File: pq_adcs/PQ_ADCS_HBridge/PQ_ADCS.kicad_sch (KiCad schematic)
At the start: 53 parts, among them J1 CES-110-02-L-S, J10 Pico-Clasp_01x09, J11 Pico-Clasp_01x15, J12 CES-102-02-L-S, J2 CES-110-02-L-S, J3 CES-110-02-L-S, J4 CES-110-02-L-S, J5 Pico-Clasp_01x03, J6 Pico-Clasp_01x10, J7 Pico-Clasp_01x10, J8 Pico-Clasp_01x10, J9 Pico-Clasp_01x10, U1 LPV542, U2 LPV542, U3 LPV542, U4 IIM-42652, U5 DRV8214RTER, U6 TMUX1108RSVR, U7 MMC5983MA, U8 DRV8214RTER, U9 DRV8214RTER

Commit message: NC digital pincs fix
Unused digital pins as well as I2C pins are now set as not connected instead of grounded. Added lock files to gitignore
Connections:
- net GND: no longer U5.3 (RC_OUT), U5.4 (~{FAULT}), U8.3 (RC_OUT), U8.4 (~{FAULT}), U9.3 (RC_OUT), U9.4 (~{FAULT})
- no-connect marks 9 -> 18

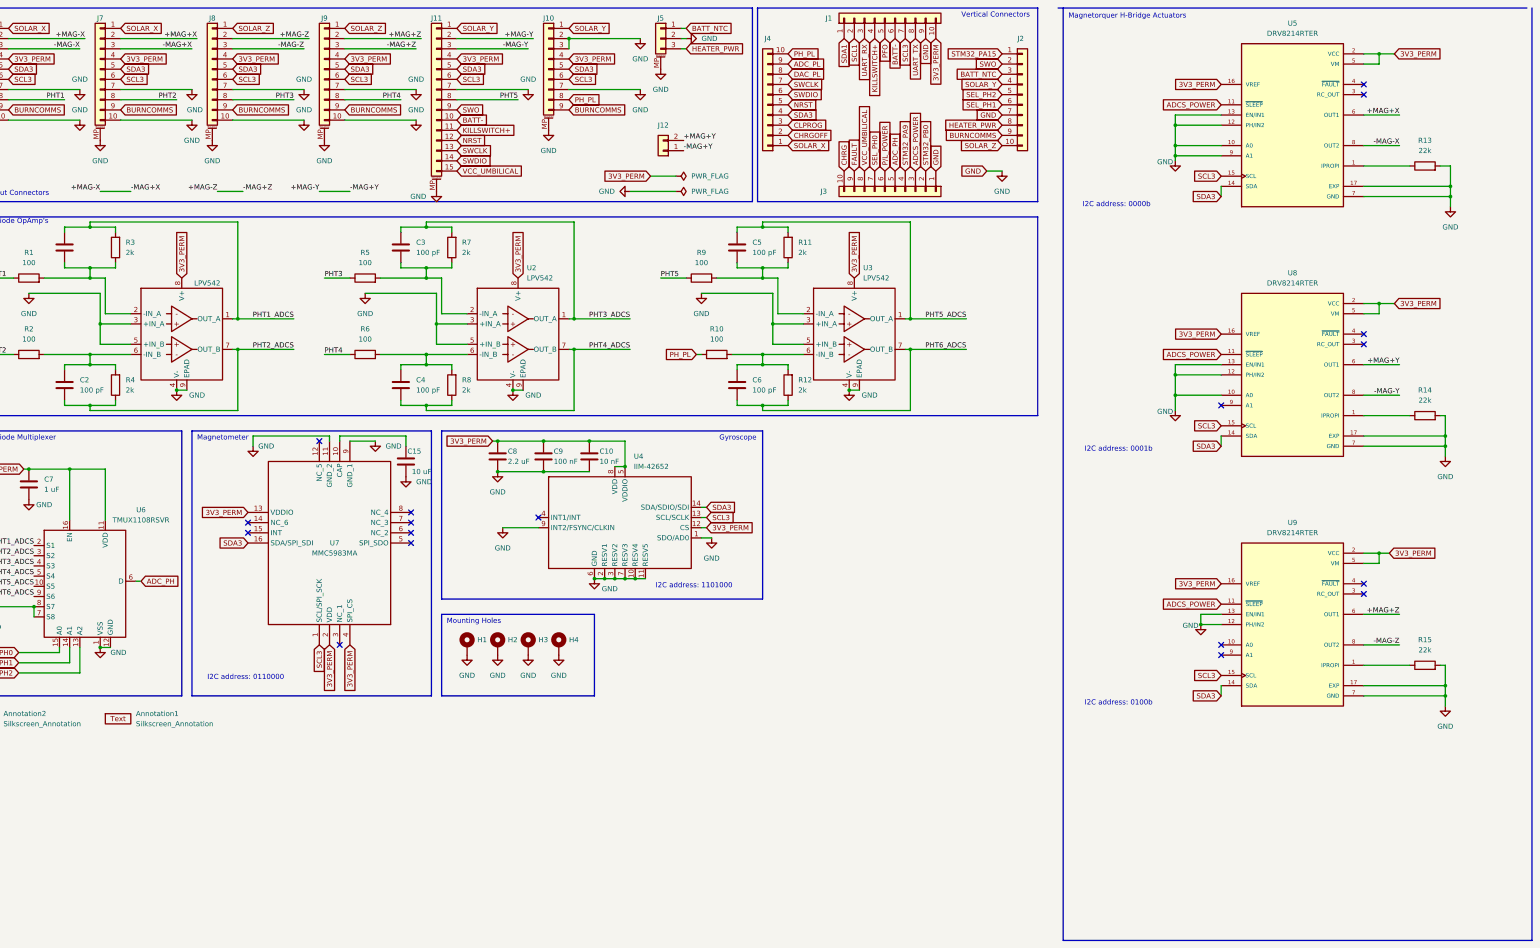
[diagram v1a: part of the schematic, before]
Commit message: Added Capacitors to HBridge Controllers
Coupling capacitors added as required by the HBridge controllers.
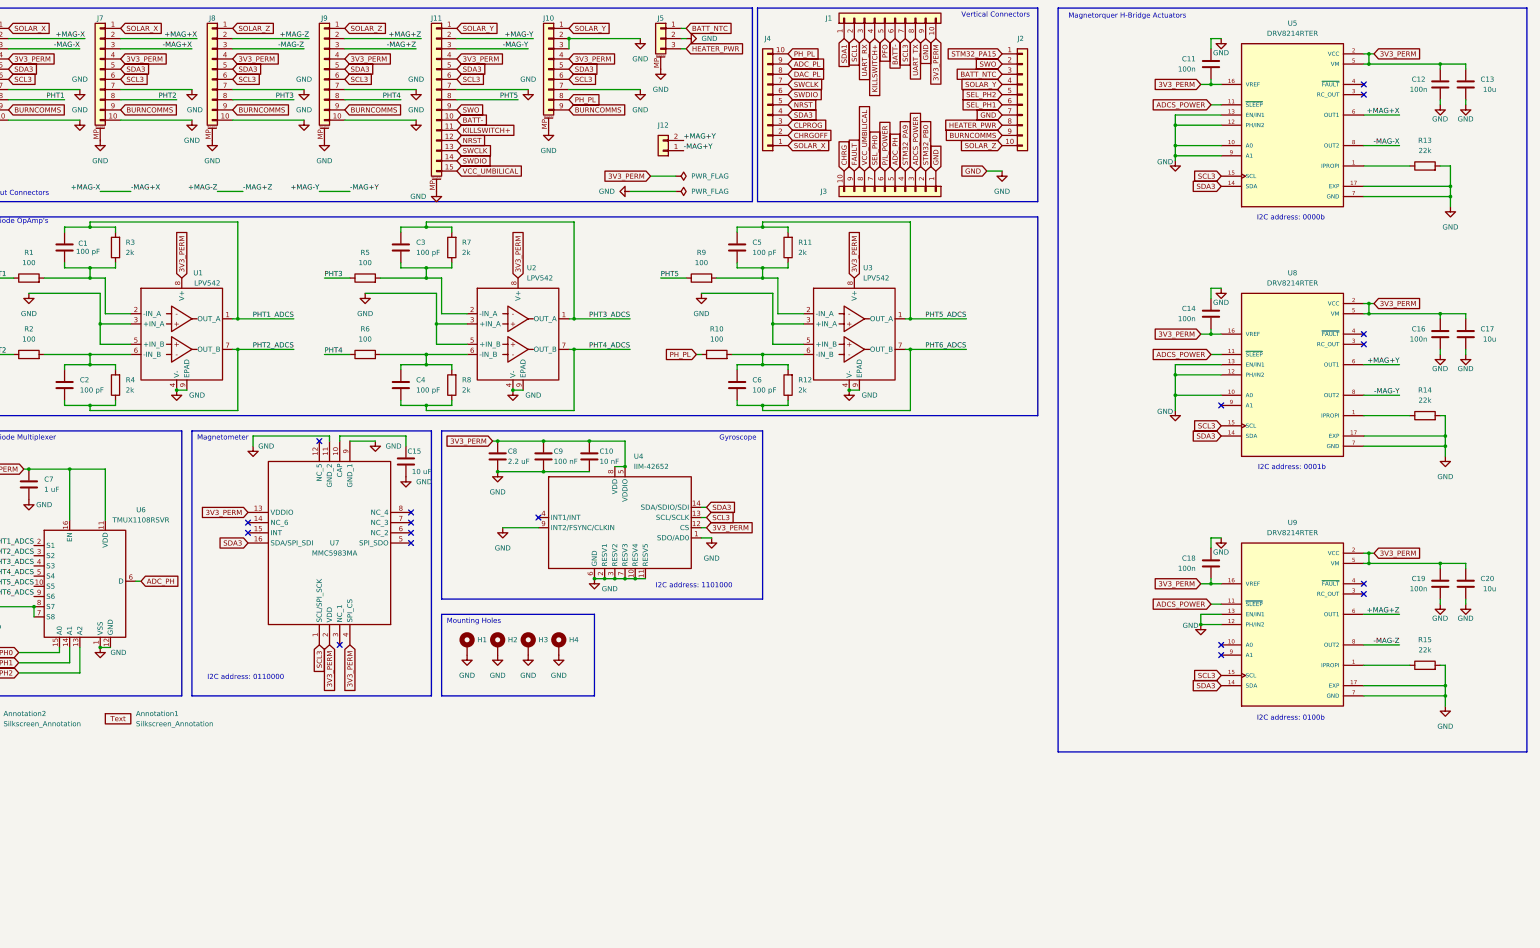
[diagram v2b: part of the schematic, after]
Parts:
- added C11, C12, C14, C16, C18, C19: 100n, Capacitor_SMD:C_0603_1608Metric, symbol Device:C
- added C13, C17, C20: 10u, Capacitor_SMD:C_0603_1608Metric, symbol Device:C
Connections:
- net 3V3_PERM: now also C11.2, C12.1, C13.1, C14.2, C16.1, C17.1, C18.2, C19.1, C20.1
- net GND: now also C11.1, C12.2, C13.2, C14.1, C16.2, C17.2, C18.1, C19.2, C20.2
